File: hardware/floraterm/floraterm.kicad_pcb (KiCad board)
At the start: 2 copper layers, 76.9 x 48.6 mm, 21 parts, among them J1 Conn_01x02_Pin, U1 TMUX1104DGSR, U2 TMUX1104DGSR, U3 LGS4084HB6, U4 TX4401

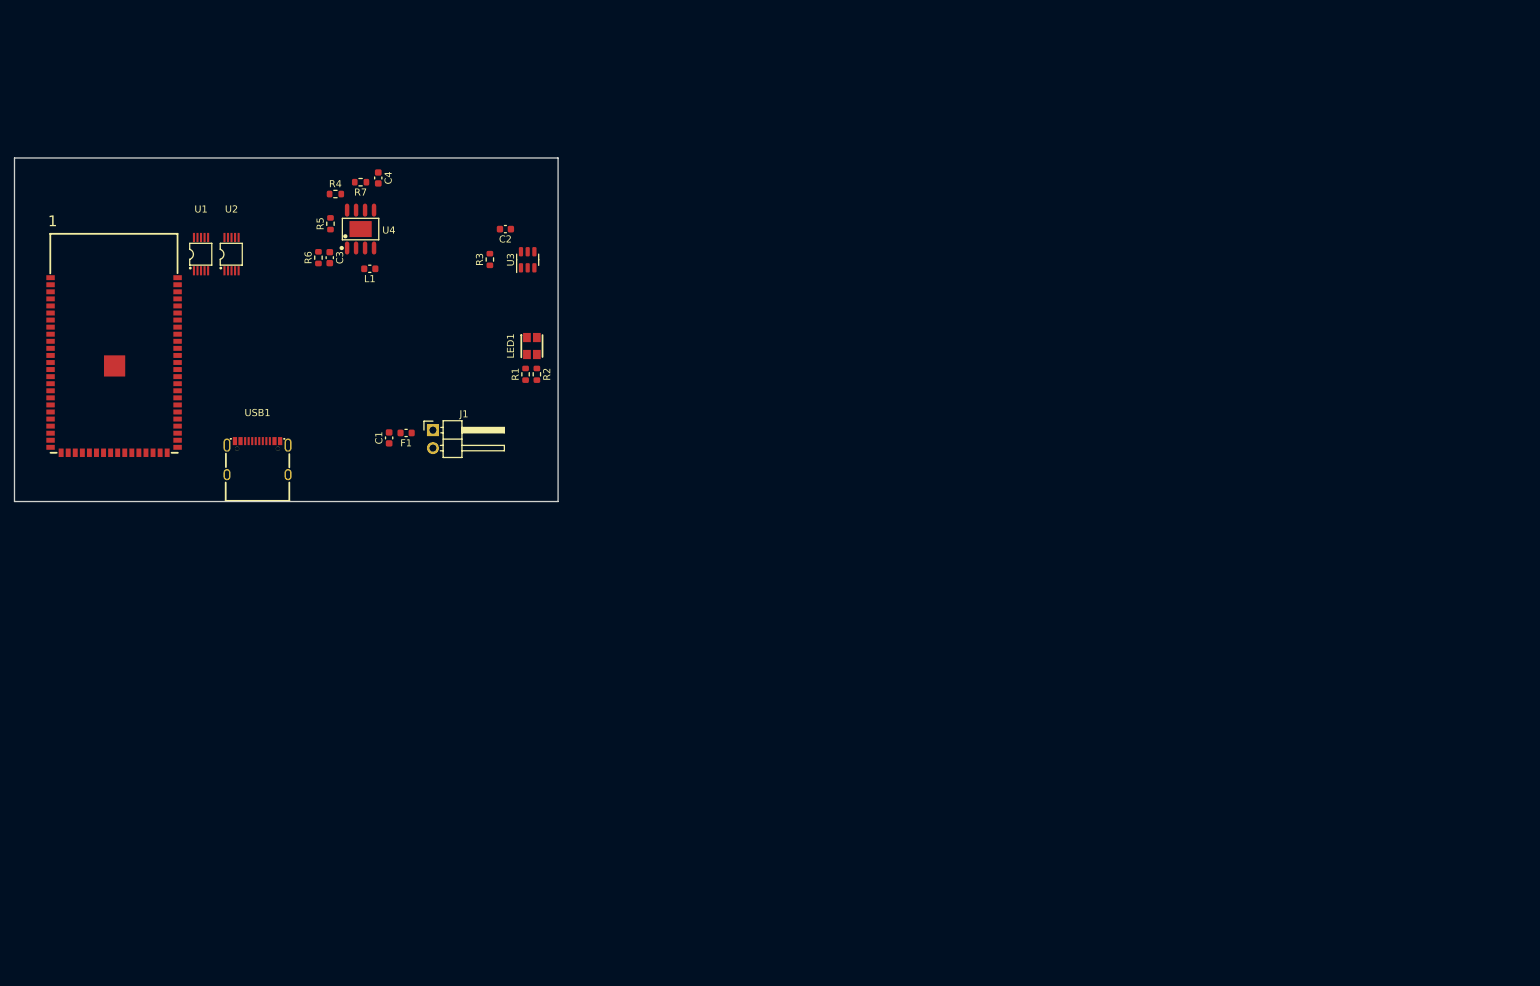
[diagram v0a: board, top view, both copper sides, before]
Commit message: add screen, keyboard and speaker
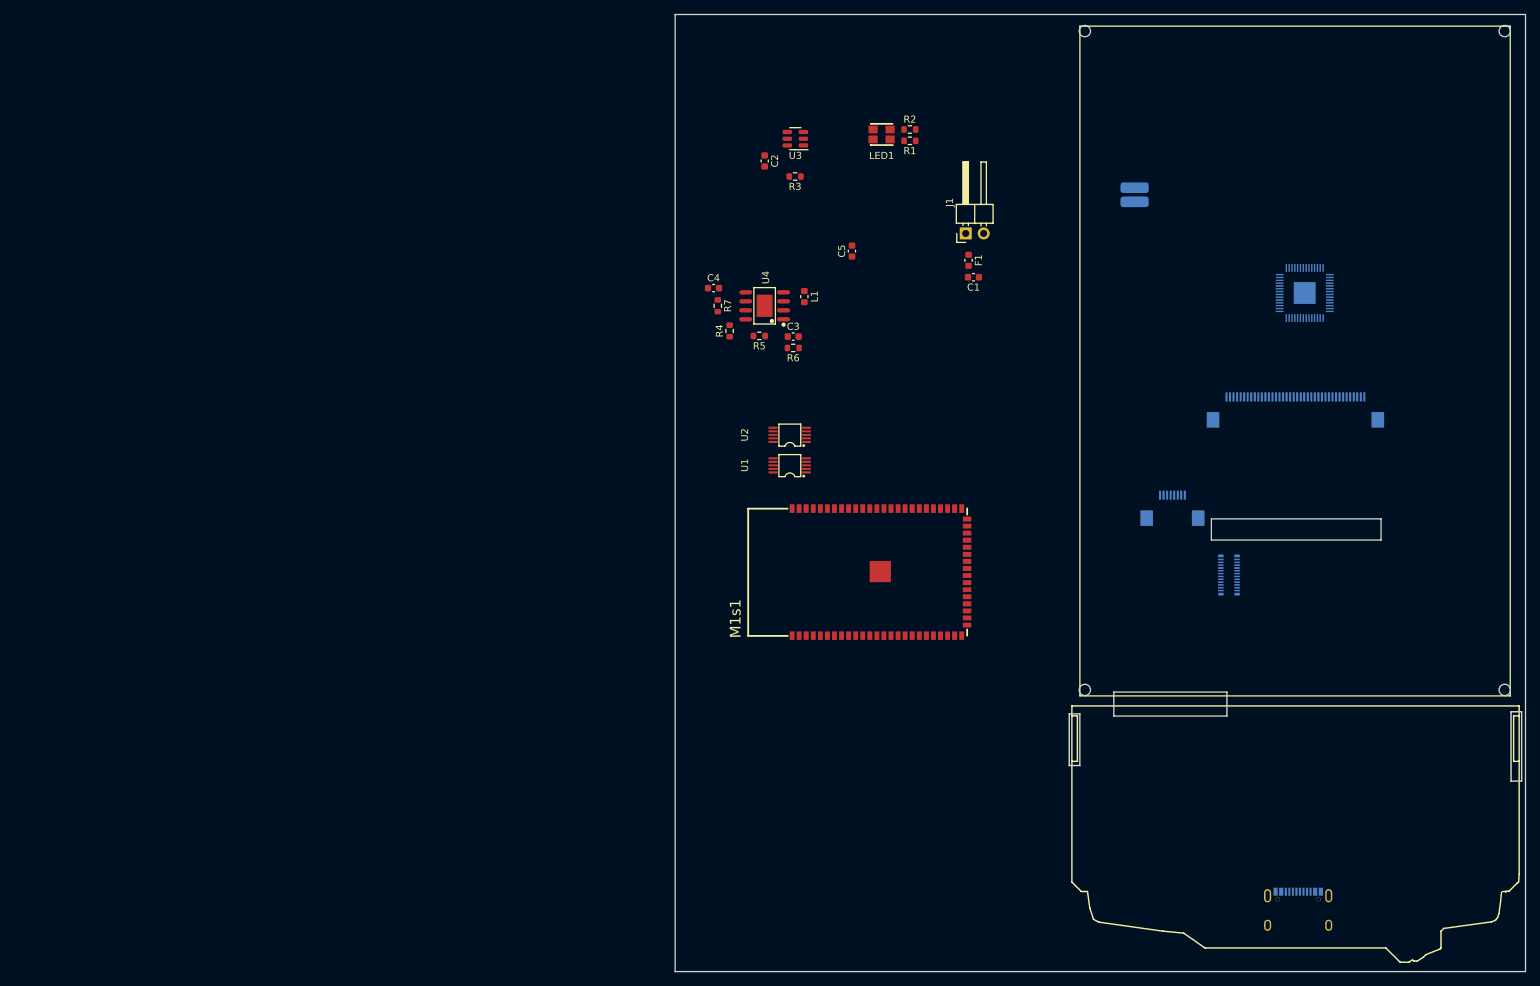
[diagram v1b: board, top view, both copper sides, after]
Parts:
- removed 1: 0_M1s, M1s:M1s
- added C5: 22uF, Capacitor_SMD:C_0603_1608Metric, F.Cu at (175.7, 56.6)
- added M1s1: 0_M1s, M1s:M1s, F.Cu at (179.6, 102.0)
- added REF**: BBQ10KBD, Keyboard:BBQ10KBD, F.Cu at (238.4, 138.0)
- added U5: RP2040, lcsc:LQFN-56_L7.0-W7.0-P0.4-EP, B.Cu at (239.7, 62.5)
- added U6: BBQ10KBD, Connector_Hirose_Extra:BM14B(0.8)-24DS-0.4V(53), B.Cu at (229.0, 102.4)
- added U7: iPhone 13 PM SPK, iphone_speaker:iphone_13_pro_max, B.Cu at (211.7, 48.6)
- added U8: ILI9488, Connector_FFC-FPC:Hirose_FH12-40S-0.5SH_1x40-1MP_P0.50mm_Horizontal, B.Cu at (238.4, 79.0)
- added U9: GT911, Connector_FFC-FPC:Hirose_FH12-8S-0.5SH_1x08-1MP_P0.50mm_Horizontal, B.Cu at (221.0, 93.0)
- USB1: moved to B.Cu
- moved USB1 160.4 mm to (238.8, 149.6), turned to 180 degrees
- moved U1 88.5 mm to (166.9, 86.9), turned to 90 degrees
- moved C1 85.7 mm to (192.9, 60.3), turned to 180 degrees
- moved F1 83.2 mm to (192.2, 57.9), turned to -90 degrees
- moved U2 83.0 mm to (166.9, 82.6), turned to 90 degrees
- moved J1 80.3 mm to (191.8, 54.1), turned to 90 degrees
- moved R6 68.4 mm to (167.4, 70.3), turned to 180 degrees
- moved C3 66.5 mm to (167.4, 68.7), turned to 0 degrees
- moved R1 63.6 mm to (183.9, 41.0), turned to 180 degrees
- moved R2 63.1 mm to (183.9, 39.4), turned to 0 degrees
- moved R5 62.7 mm to (162.6, 68.6), turned to 180 degrees
- moved L1 61.6 mm to (168.9, 63.0), turned to -90 degrees
- moved R4 59.0 mm to (158.4, 67.9), turned to 90 degrees
- moved U4 58.2 mm to (163.3, 64.3), turned to 90 degrees
- moved LED1 57.8 mm to (179.9, 40.1), turned to 180 degrees
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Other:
- board size 76.9 x 48.6 mm -> 120.3 x 135.4 mm
